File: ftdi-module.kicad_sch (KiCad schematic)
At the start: 58 parts

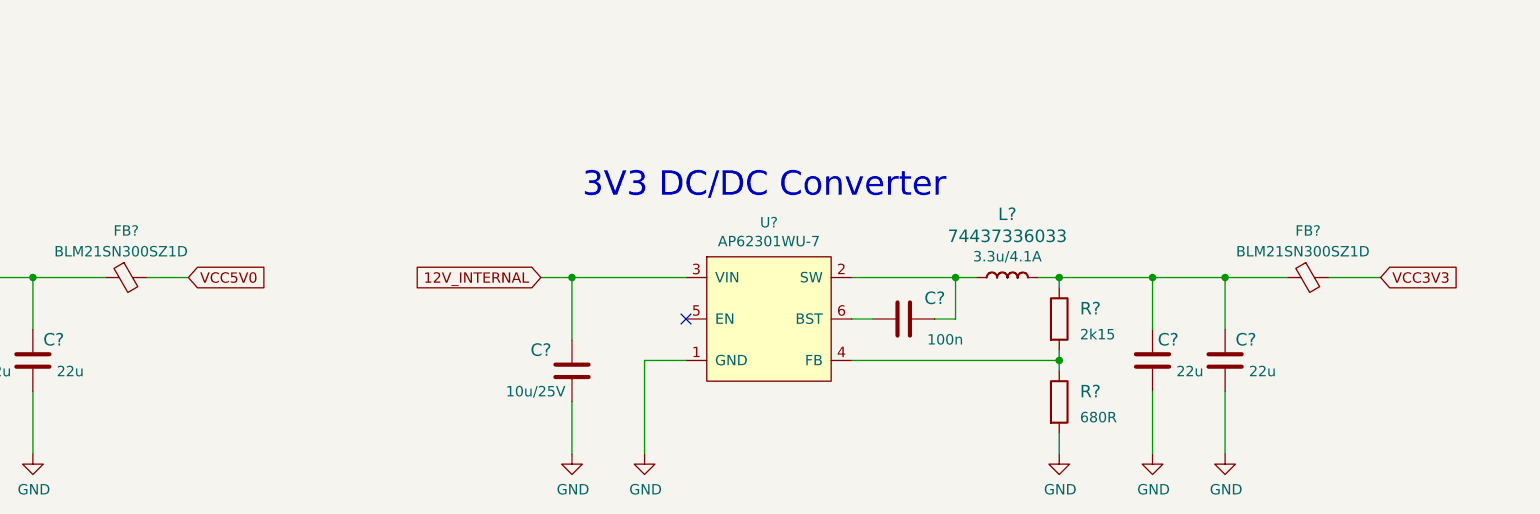
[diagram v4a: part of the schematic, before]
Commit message: Rearrange pwr flags
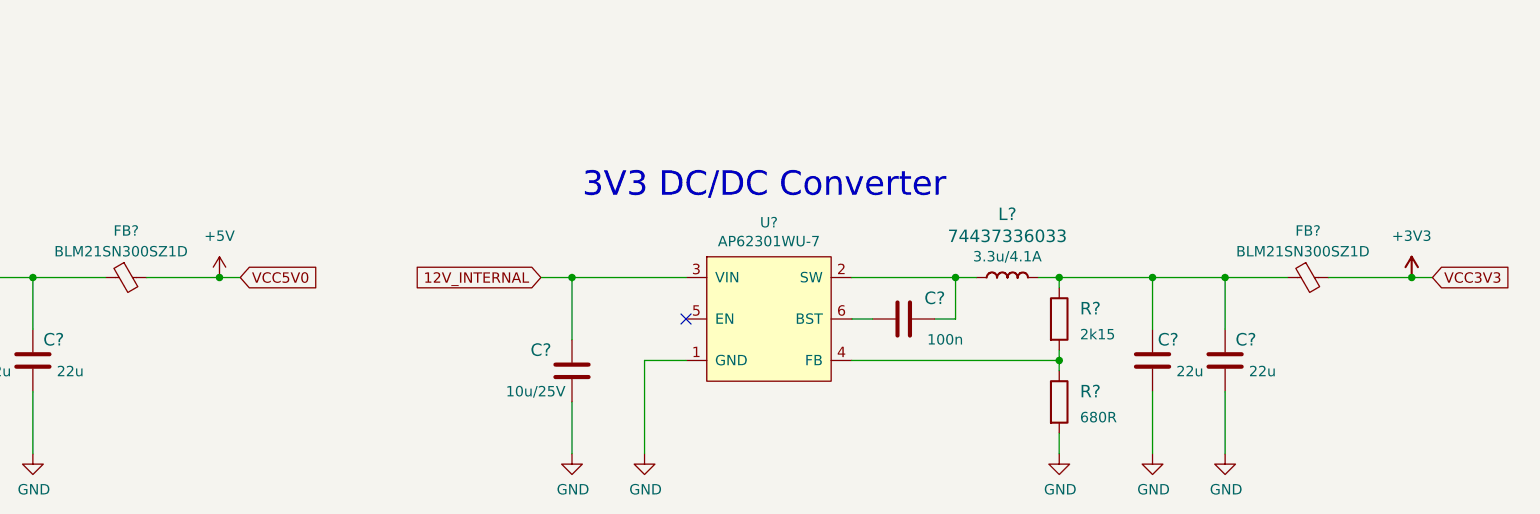
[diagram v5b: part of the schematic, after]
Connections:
- net VCC3V3 renamed +3V3
- net VCC5V0 renamed +5V
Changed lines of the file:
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@@
   (junction (at 96.52 66.04) (diameter 0) (color 0 0 0 0)
   )
+  (junction (at 314.96 199.39) (diameter 0) (color 0 0 0 0)
+  )
   (junction (at 292.1 199.39) (diameter 0) (color 0 0 0 0)
   )
@@
   (junction (at 212.09 199.39) (diameter 0) (color 0 0 0 0)
   )
+  (junction (at 168.91 199.39) (diameter 0) (color 0 0 0 0)
+  )
   (junction (at 196.85 53.34) (diameter 0) (color 0 0 0 0)
   )
@@
     (stroke (width 0) (type default) (color 0 0 0 0))
   )
+  (wire (pts (xy 314.96 199.39) (xy 317.5 199.39))
+    (stroke (width 0) (type default) (color 0 0 0 0))
+  )
   (wire (pts (xy 210.82 93.98) (xy 218.44 93.98))
     (stroke (width 0) (type default) (color 0 0 0 0))
@@
     (stroke (width 0) (type default) (color 0 0 0 0))
   )
+  (wire (pts (xy 168.91 199.39) (xy 171.45 199.39))
+    (stroke (width 0) (type default) (color 0 0 0 0))
+  )
   (wire (pts (xy 176.53 77.47) (xy 193.04 77.47))
     (stroke (width 0) (type default) (color 0 0 0 0))
@@
     (stroke (width 0) (type default) (color 0 0 0 0))
   )
-  (wire (pts (xy 160.02 199.39) (xy 165.1 199.39))
+  (wire (pts (xy 160.02 199.39) (xy 168.91 199.39))
     (stroke (width 0) (type default) (color 0 0 0 0))
   )
@@
     (stroke (width 0) (type default) (color 0 0 0 0))
   )
-  (wire (pts (xy 304.8 199.39) (xy 311.15 199.39))
+  (wire (pts (xy 304.8 199.39) (xy 314.96 199.39))
     (stroke (width 0) (type default) (color 0 0 0 0))
   )
@@
     )
   )
-  (global_label "VCC3V3" (shape input) (at 311.15 199.39 0) (fields_autoplaced)
+  (global_label "VCC3V3" (shape input) (at 317.5 199.39 0) (fields_autoplaced)
     (effects (font (size 1.27 1.27)) (justify left))
-    (property "Intersheet References" "${INTERSHEET_REFS}" (id 0) (at 161.925 97.79 0)
+    (property "Intersheet References" "${INTERSHEET_REFS}" (id 0) (at 168.275 97.79 0)
       (effects (font (size 1.27 1.27)) hide)
     )
@@
     )
   )
-  (global_label "VCC5V0" (shape input) (at 165.1 199.39 0) (fields_autoplaced)
+  (global_label "VCC5V0" (shape input) (at 171.45 199.39 0) (fields_autoplaced)
     (effects (font (size 1.27 1.27)) (justify left))
-    (property "Intersheet References" "${INTERSHEET_REFS}" (id 0) (at 174.5604 199.3106 0)
+    (property "Intersheet References" "${INTERSHEET_REFS}" (id 0) (at 180.9104 199.3106 0)
       (effects (font (size 1.27 1.27)) (justify left) hide)
     )
@@
     (pin "2")
   )
+  (symbol (lib_id "antmicropower:+3V3") (at 314.96 199.39 0) (unit 1)
+    (in_bom yes) (on_board yes) (fields_autoplaced)
+    (property "Reference" "#PWR?" (id 0) (at 330.2 201.93 0)
+      (effects (font (size 1.27 1.27) (thickness 0.15)) (justify left bottom) hide)
+    )
+    (property "Value" "+3V3" (id 1) (at 314.96 194.31 0)
+      (effects (font (size 1.27 1.27) (thickness 0.15)))
+    )
+    (property "Footprint" "" (id 2) (at 330.2 207.01 0)
+      (effects (font (size 1.27 1.27) (thickness 0.15)) (justify left bottom) hide)
+    )
+    (property "Datasheet" "" (id 3) (at 330.2 209.55 0)
+      (effects (font (size 1.27 1.27) (thickness 0.15)) (justify left bottom) hide)
+    )
+    (property "Author" "Antmicro" (id 4) (at 330.2 207.01 0)
+      (effects (font (size 1.27 1.27) (thickness 0.15)) (justify left bottom) hide)
+    )
+    (property "License" "Apache-2.0" (id 5) (at 330.2 209.55 0)
+      (effects (font (size 1.27 1.27) (thickness 0.15)) (justify left bottom) hide)
+    )
+    (pin "1")
+  )
   (symbol (lib_id "d1600e-psu-breakout-board:74437336033") (at 119.38 199.39 0) (unit 1)
     (in_bom yes) (on_board yes)
@@
     (pin "2")
   )
+  (symbol (lib_id "antmicropower:+5V") (at 168.91 199.39 0) (unit 1)
+    (in_bom yes) (on_board yes) (fields_autoplaced)
+    (property "Reference" "#PWR?" (id 0) (at 184.15 201.93 0)
+      (effects (font (size 1.27 1.27) (thickness 0.15)) (justify left bottom) hide)
+    )
+    (property "Value" "+5V" (id 1) (at 168.91 194.31 0)
+      (effects (font (size 1.27 1.27) (thickness 0.15)))
+    )
+    (property "Footprint" "" (id 2) (at 184.15 207.01 0)
+      (effects (font (size 1.27 1.27) (thickness 0.15)) (justify left bottom) hide)
+    )
+    (property "Datasheet" "" (id 3) (at 184.15 209.55 0)
+      (effects (font (size 1.27 1.27) (thickness 0.15)) (justify left bottom) hide)
+    )
+    (property "Author" "Antmicro" (id 4) (at 184.15 207.01 0)
+      (effects (font (size 1.27 1.27) (thickness 0.15)) (justify left bottom) hide)
+    )
+    (property "License" "Apache-2.0" (id 5) (at 184.15 209.55 0)
+      (effects (font (size 1.27 1.27) (thickness 0.15)) (justify left bottom) hide)
+    )
+    (pin "1")
+  )
   (symbol (lib_id "d1600e-psu-breakout-board:GND") (at 125.73 220.98 0) (unit 1)

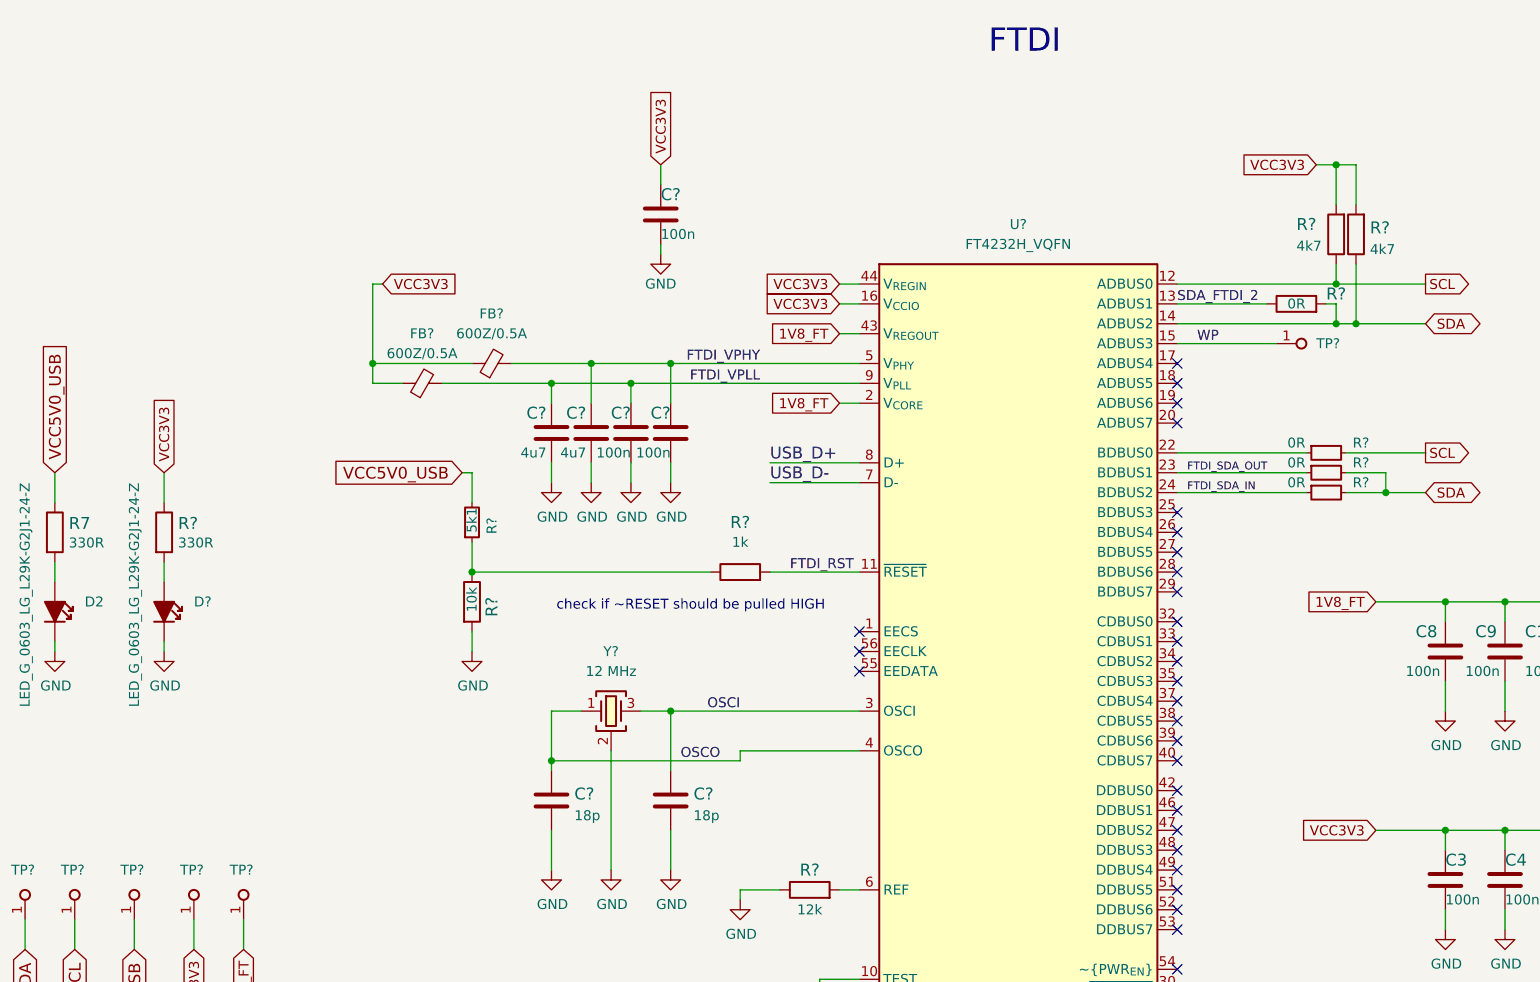
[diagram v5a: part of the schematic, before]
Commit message: Change power flags on schematic
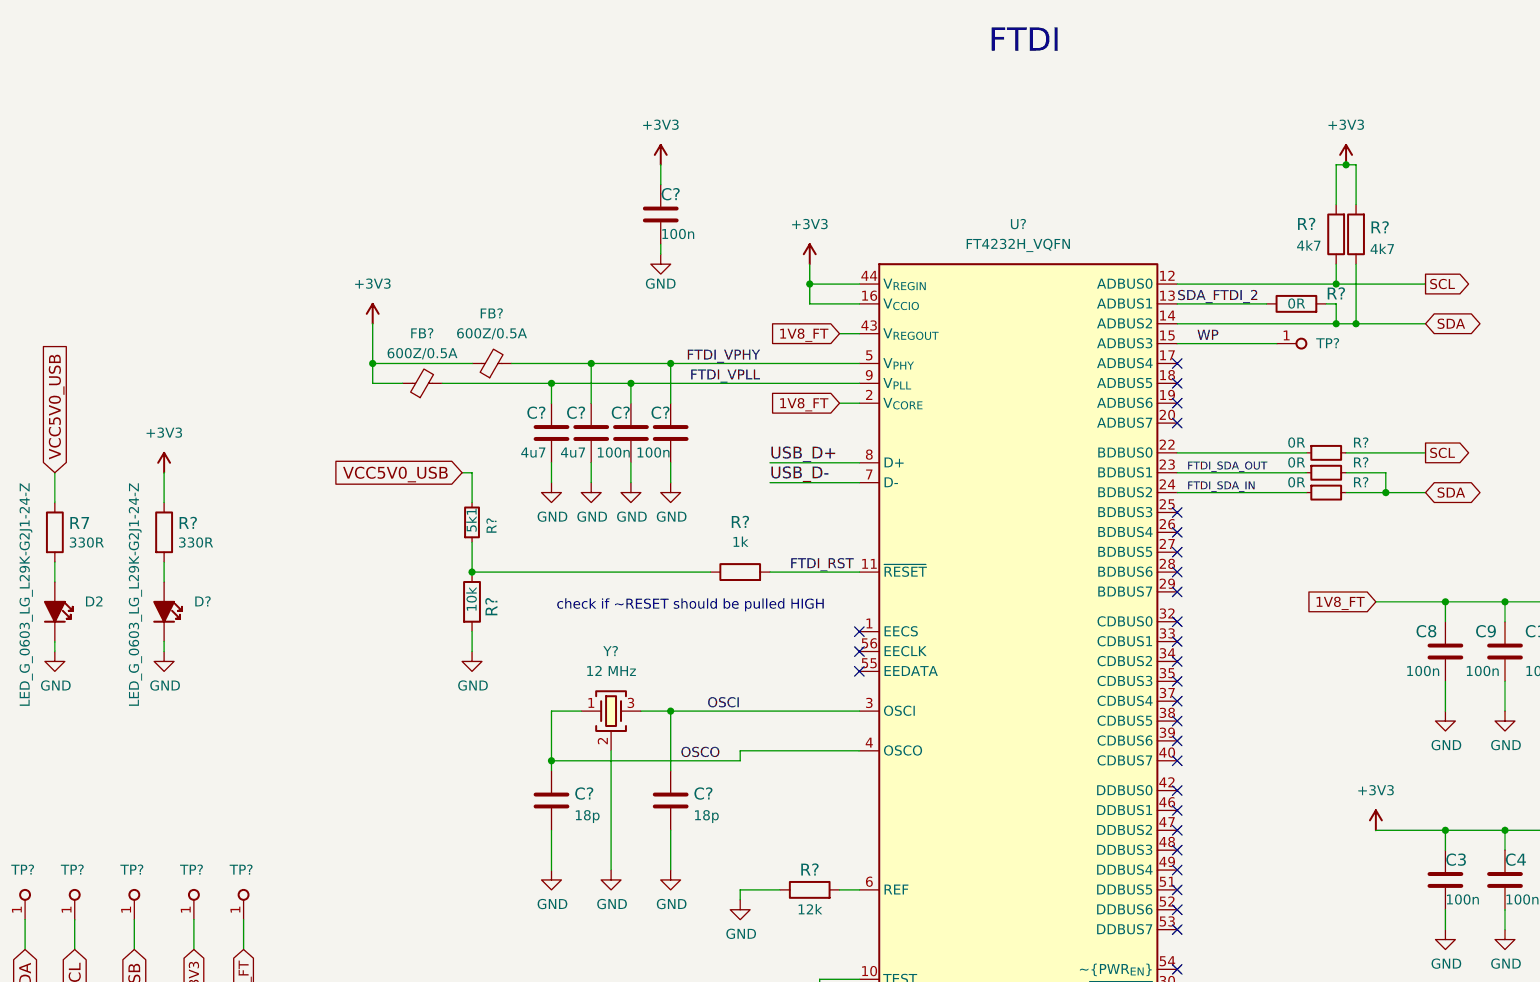
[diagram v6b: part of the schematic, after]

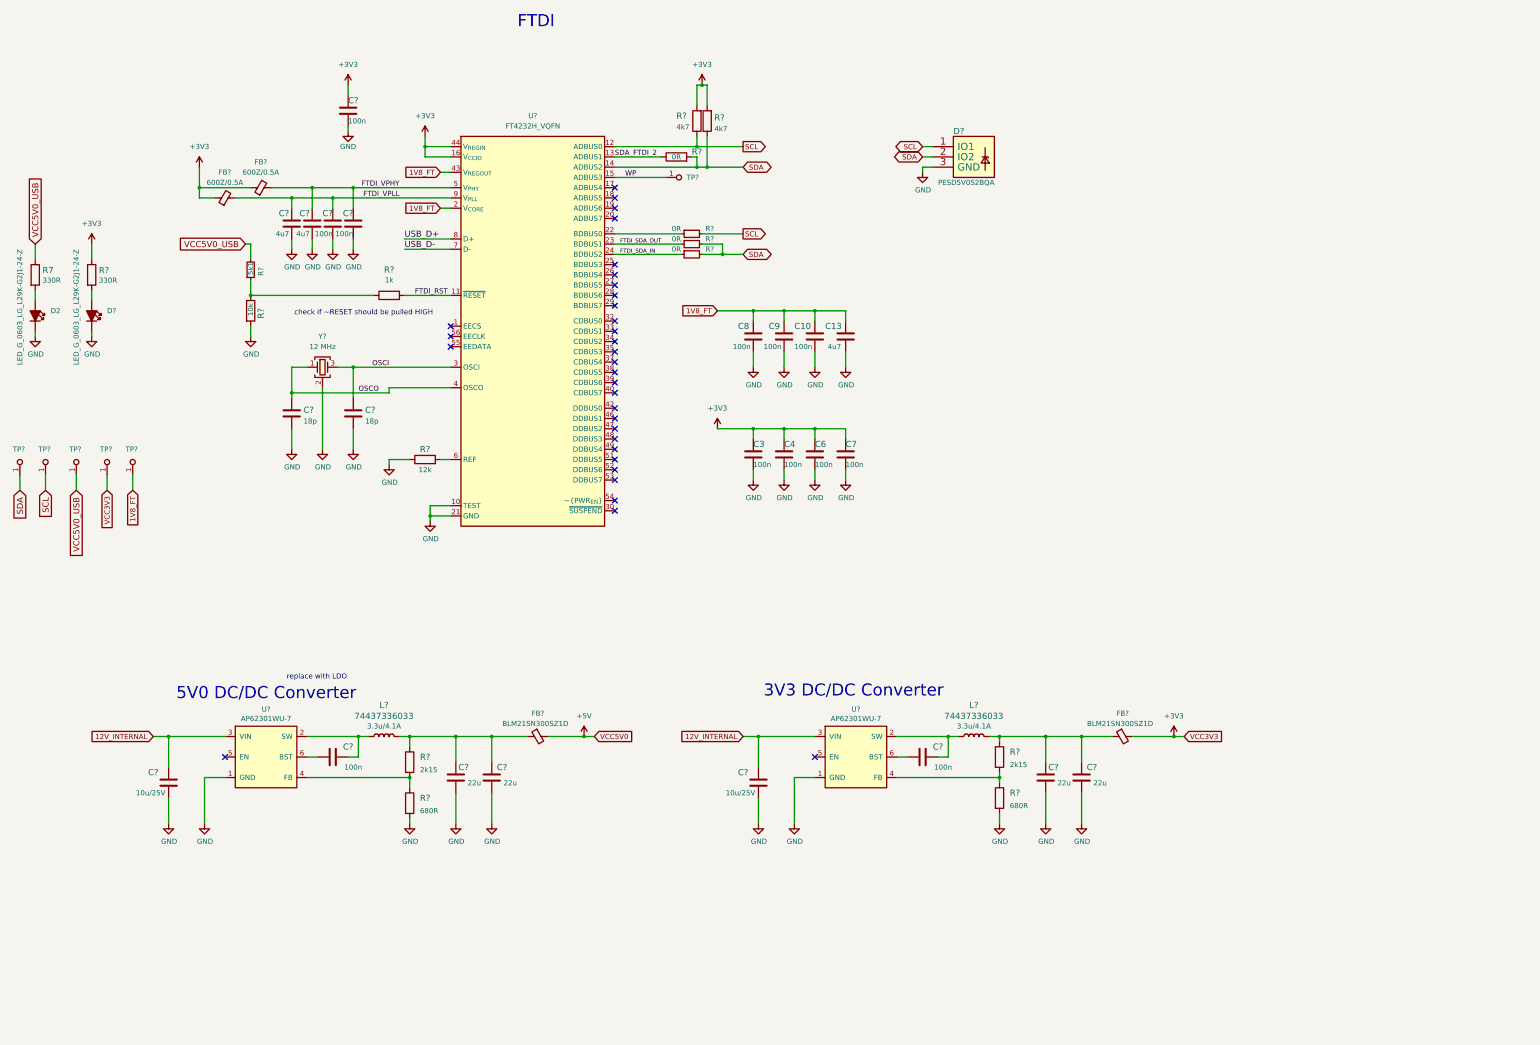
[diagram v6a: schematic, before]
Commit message: Reannotate schematic symbols
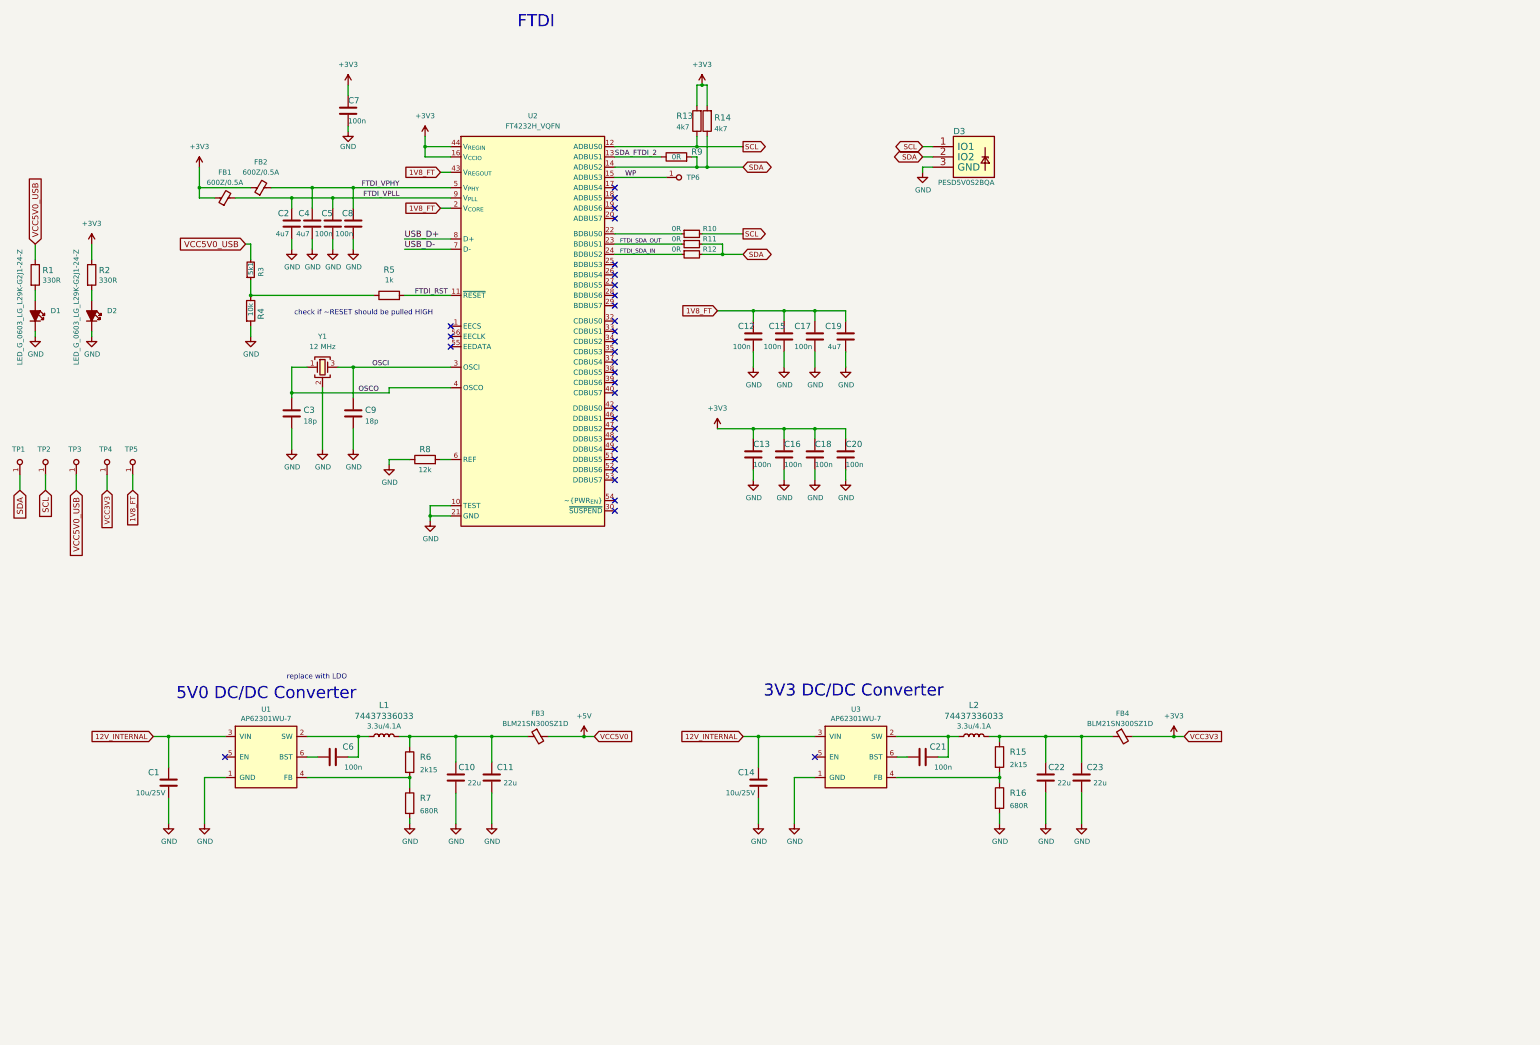
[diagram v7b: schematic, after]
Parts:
- gave numbers to parts that had none: 48
- renumbered C8 to C12, C3 to C13, C9 to C15, C4 to C16, C10 to C17, C6 to C18, C13 to C19, C7 to C20, D2 to D1, R7 to R1
